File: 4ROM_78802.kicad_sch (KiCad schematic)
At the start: 7 parts, among them J1 27C256, J2 4ROM_100_prog, U1 SST39SF010A

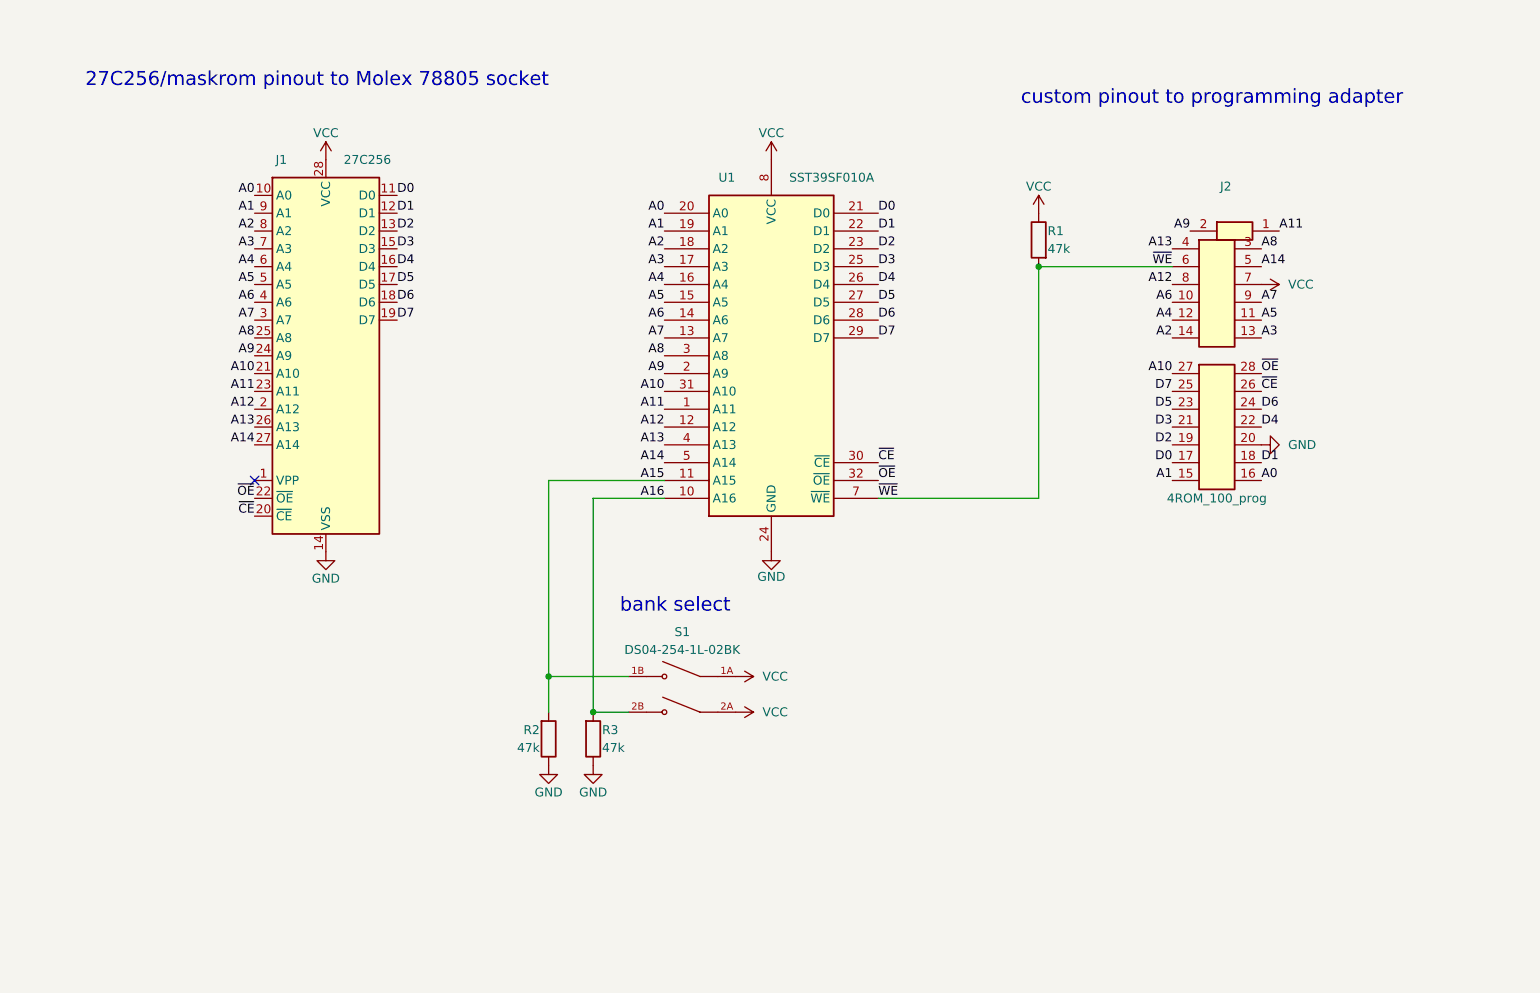
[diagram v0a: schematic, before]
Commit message: 4ROM_78802 and programming adapter are now tested and verified
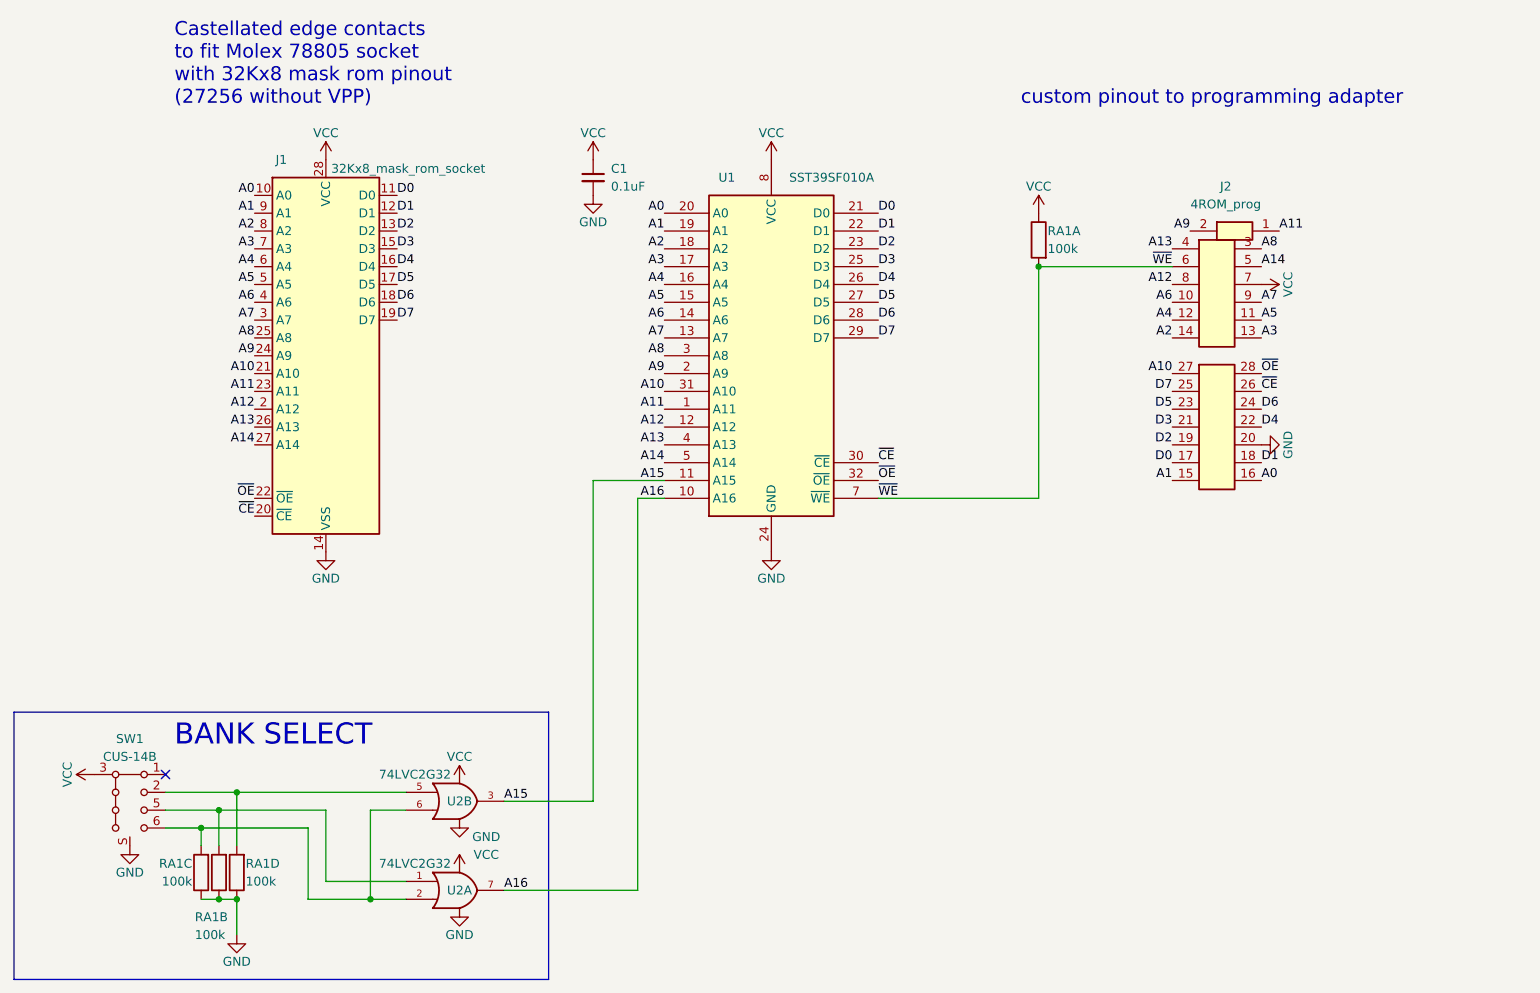
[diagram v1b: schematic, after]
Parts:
- removed R1, R2, R3: 47k, 000_LOCAL:R_0805, symbol 000_LOCAL:R
- removed S1: DS04-254-1L-02BK, 000_LOCAL:SW_DS04-254-1L-02BK, symbol 000_LOCAL:DS04-254-1L-02BK
- added C1: 0.1uF, 000_LOCAL:C_0805, symbol 000_LOCAL:C
- added RA1: 100k, 000_LOCAL:R_Array_Convex_4x0612, symbol 000_LOCAL:R_Array_04
- added SW1: CUS-14B, 000_LOCAL:SW_SP4T_CUS-14B, symbol 000_LOCAL:SW_1P4T_CUS-14B
- added U2: 74LVC2G32, 000_LOCAL:TSSOP-8_3x3mm_P0.65mm, symbol 000_LOCAL:74LVC2G32
- J1: value 27C256 -> 32Kx8_mask_rom_socket; symbol 000_LOCAL:27C256 -> 000_LOCAL:32Kx8_mask_rom_socket
- J2: value 4ROM_100_prog -> 4ROM_prog; footprint 000_LOCAL:4ROM_100_prog_female -> 000_LOCAL:4ROM_prog_female; symbol 000_LOCAL:4ROM_100_prog -> 000_LOCAL:4ROM_prog
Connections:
- net A15: now also U2.3
- net A16: now also U2.7
- net GND: now also C1.2, RA1.5 (R4.2), RA1.6 (R3.2), RA1.7 (R2.2), SW1.S, U2.4 (GND), U2.4 (GND)
- net VCC: now also C1.1, RA1.8 (R1.2), SW1.3 (C), SW1.4 (C), U2.8 (VCC), U2.8 (VCC)
- net ~{WE}: now also RA1.1 (R1.1)
- new net: RA1.4 (R4.1), SW1.2, U2.5
- new net: RA1.2 (R2.1), SW1.5, U2.1
- new net: RA1.3 (R3.1), SW1.6, U2.2, U2.6
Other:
- note added: "BANK SELECT"
- note added: "Castellated edge contacts to fit Molex 78805 socket with 32Kx8 mask rom pinout (27256 without VPP)"
- note removed: "27C256/maskrom pinout to Molex 78805 socket"
- note removed: "bank select"
- title: 4ROM_STD -> 4ROM_78802

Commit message: cosmetic schematic touchups
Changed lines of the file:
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@@
       (effects (font (size 1.27 1.27)) hide)
     )
-    (property "Value" "VCC" (id 1) (at 52.07 148.59 0))
+    (property "Value" "VCC" (id 1) (at 50.8 148.59 90))
     (property "Footprint" "" (id 2) (at 55.88 148.59 0)
       (effects (font (size 1.27 1.27)) hide)
     )
     (property "Datasheet" "" (id 3) (at 55.88 148.59 0)
-      (effects (font (size 1.27 1.27)) hide)
-    )
-    (pin "1")
-  )
-  (symbol (lib_id "000_LOCAL:VCC") (at 107.95 149.86 0) (mirror y) (unit 1)
-    (in_bom yes) (on_board yes)
-    (property "Reference" "#PWR0109" (id 0) (at 107.95 153.67 0)
-      (effects (font (size 1.27 1.27)) hide)
-    )
-    (property "Value" "VCC" (id 1) (at 107.95 146.05 0))
-    (property "Footprint" "" (id 2) (at 107.95 149.86 0)
-      (effects (font (size 1.27 1.27)) hide)
-    )
-    (property "Datasheet" "" (id 3) (at 107.95 149.86 0)
       (effects (font (size 1.27 1.27)) hide)
     )
@@
     (pin "6")
   )
-  (symbol (lib_id "000_LOCAL:GND") (at 107.95 167.64 0) (mirror y) (unit 1)
-    (in_bom yes) (on_board yes)
-    (property "Reference" "#PWR0112" (id 0) (at 107.95 171.45 0)
-      (effects (font (size 1.27 1.27)) hide)
-    )
-    (property "Value" "GND" (id 1) (at 107.95 171.45 0))
-    (property "Footprint" "" (id 2) (at 107.95 167.64 0)
-      (effects (font (size 1.27 1.27)) hide)
-    )
-    (property "Datasheet" "" (id 3) (at 107.95 167.64 0)
-      (effects (font (size 1.27 1.27)) hide)
-    )
-    (pin "1")
-  )
   (symbol (lib_id "000_LOCAL:GND") (at 127 66.04 0) (unit 1)
     (in_bom yes) (on_board yes)
@@
     )
     (property "Datasheet" "" (id 3) (at 60.96 158.75 0)
-      (effects (font (size 1.27 1.27)) hide)
-    )
-    (pin "1")
-  )
-  (symbol (lib_id "000_LOCAL:GND") (at 107.95 154.94 0) (mirror y) (unit 1)
-    (in_bom yes) (on_board yes)
-    (property "Reference" "#PWR0106" (id 0) (at 107.95 158.75 0)
-      (effects (font (size 1.27 1.27)) hide)
-    )
-    (property "Value" "GND" (id 1) (at 111.76 157.48 0))
-    (property "Footprint" "" (id 2) (at 107.95 154.94 0)
-      (effects (font (size 1.27 1.27)) hide)
-    )
-    (property "Datasheet" "" (id 3) (at 107.95 154.94 0)
       (effects (font (size 1.27 1.27)) hide)
     )
@@
       (effects (font (size 1.27 1.27)) hide)
     )
-    (property "Value" "VCC" (id 1) (at 226.06 78.74 0))
+    (property "Value" "VCC" (id 1) (at 227.33 78.74 90))
     (property "Footprint" "" (id 2) (at 222.25 78.74 0)
       (effects (font (size 1.27 1.27)) hide)
@@
     (pin "9")
   )
-  (symbol (lib_id "000_LOCAL:VCC") (at 107.95 162.56 0) (mirror y) (unit 1)
-    (in_bom yes) (on_board yes)
-    (property "Reference" "#PWR0113" (id 0) (at 107.95 166.37 0)
-      (effects (font (size 1.27 1.27)) hide)
-    )
-    (property "Value" "VCC" (id 1) (at 111.76 160.02 0))
-    (property "Footprint" "" (id 2) (at 107.95 162.56 0)
-      (effects (font (size 1.27 1.27)) hide)
-    )
-    (property "Datasheet" "" (id 3) (at 107.95 162.56 0)
-      (effects (font (size 1.27 1.27)) hide)
-    )
-    (pin "1")
-  )
   (symbol (lib_id "000_LOCAL:GND") (at 222.25 101.6 90) (unit 1)
     (in_bom yes) (on_board yes)
@@
       (effects (font (size 1.27 1.27)) hide)
     )
-    (property "Value" "GND" (id 1) (at 226.06 101.6 0))
+    (property "Value" "GND" (id 1) (at 227.33 101.6 90))
     (property "Footprint" "" (id 2) (at 222.25 101.6 0)
       (effects (font (size 1.27 1.27)) hide)
@@
       (reference "#PWR0105") (unit 1) (value "VCC") (footprint "")
     )
-    (path "/99de4d92-1621-4226-ad5a-9c332f9b8683"
-      (reference "#PWR0106") (unit 1) (value "GND") (footprint "")
-    )
     (path "/00000000-0000-0000-0000-00005fa2eef3"
       (reference "#PWR0107") (unit 1) (value "GND") (footprint "")
@@
       (reference "#PWR0108") (unit 1) (value "VCC") (footprint "")
     )
-    (path "/00000000-0000-0000-0000-00005fa17c43"
-      (reference "#PWR0109") (unit 1) (value "VCC") (footprint "")
-    )
     (path "/bfb01695-8269-426c-a716-e41efe9a2b4b"
       (reference "#PWR0110") (unit 1) (value "VCC") (footprint "")
@@
       (reference "#PWR0111") (unit 1) (value "GND") (footprint "")
     )
-    (path "/54e08087-1139-47a4-bc9c-ad9027759553"
-      (reference "#PWR0112") (unit 1) (value "GND") (footprint "")
-    )
-    (path "/d01540e5-2327-453c-b219-6f902db33d82"
-      (reference "#PWR0113") (unit 1) (value "VCC") (footprint "")
-    )
     (path "/842c04d7-a9d0-436a-9fdb-39b9f2756034"
